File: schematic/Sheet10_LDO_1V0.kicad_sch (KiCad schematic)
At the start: 8 parts, among them U8 TPS7H1111-SP

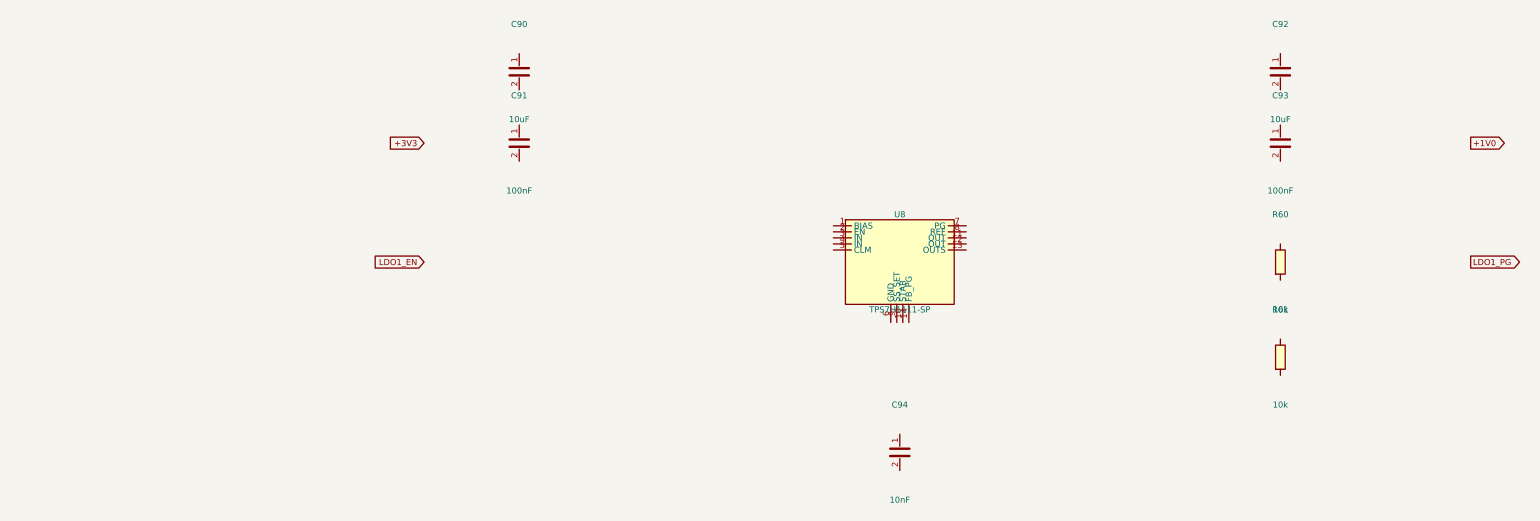
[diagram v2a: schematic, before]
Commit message: feat: add 745 wire connections linking all IC pins to labels and power symbols
- Added stub wires from every component pin to net labels/global_labels
- Power pins connected to correct power symbols (GND, +1V0, +1V8, +3V3, etc.)
- Signal pins connected to labeled nets matching design spec
- Global labels for cross-sheet signals (JESD, SPI, clock, SpaceWire)
- Fixed missing +3V3 power symbol definitions in 5 sheets
- All 17 sheets export successfully with KiCad CLI (17/17 OK)
- Merged PDF: 3.1MB, 17 pages with visible wire connections
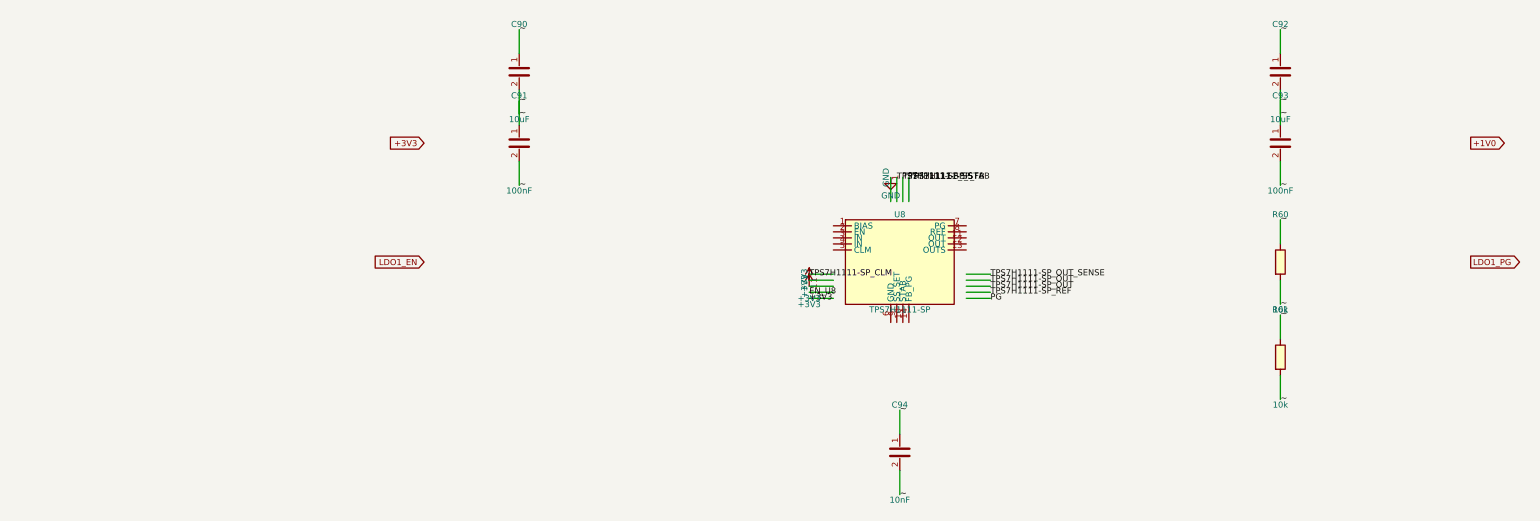
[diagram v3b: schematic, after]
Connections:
- net ~: now reaches C91.1
- net ~: now also C90.1, C90.2, C91.2, C92.1, C92.2, C93.1, C93.2, C94.1, C94.2, R60.1, R60.2, R61.1, R61.2
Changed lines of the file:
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@@
     (pin "1")
     (pin "2")
-  )  (global_label "+3V3" (shape input) (at 100 55 180) (effects (font (size 1.27 1.27)) (justify right)))  (global_label "+1V0" (shape output) (at 320 55 0) (effects (font (size 1.27 1.27)) (justify left)))  (global_label "LDO1_EN" (shape input) (at 100 80 180) (effects (font (size 1.27 1.27)) (justify right)))  (global_label "LDO1_PG" (shape output) (at 320 80 0) (effects (font (size 1.27 1.27)) (justify left)))  (sheet_instances (path "/" (page "1")))
+  )  (global_label "+3V3" (shape input) (at 100 55 180) (effects (font (size 1.27 1.27)) (justify right)))  (global_label "+1V0" (shape output) (at 320 55 0) (effects (font (size 1.27 1.27)) (justify left)))  (global_label "LDO1_EN" (shape input) (at 100 80 180) (effects (font (size 1.27 1.27)) (justify right)))  (global_label "LDO1_PG" (shape output) (at 320 80 0) (effects (font (size 1.27 1.27)) (justify left)))
+  (wire (pts (xy 186.03 87.62) (xy 180.95 87.62)) (stroke (width 0) (type default)))
+  (label "+3V3" (at 180.95 87.62 0) (effects (font (size 1.27 1.27))))
+  (wire (pts (xy 186.03 86.35) (xy 180.95 86.35)) (stroke (width 0) (type default)))
+  (label "EN_U8" (at 180.95 86.35 0) (effects (font (size 1.27 1.27))))
+  (wire (pts (xy 186.03 85.08) (xy 180.95 85.08)) (stroke (width 0) (type default)))
+  (symbol (lib_id "power:+3V3") (at 180.95 85.08 0) (unit 1)
+      (in_bom yes) (on_board yes) (dnp no)
+      (property "Reference" "#PWR6b4" (at 180.95 81.27 0) (effects (font (size 1.27 1.27)) hide))
+      (property "Value" "+3V3" (at 180.95 88.89 0) (effects (font (size 1.27 1.27))))
+      (property "Footprint" "" (at 0 0 0) (effects (font (size 1.27 1.27)) hide))
+      (property "Datasheet" "" (at 0 0 0) (effects (font (size 1.27 1.27)) hide))
+      (pin "1")
+    )
+  (wire (pts (xy 186.03 83.81) (xy 180.95 83.81)) (stroke (width 0) (type default)))
+  (symbol (lib_id "power:+3V3") (at 180.95 83.81 0) (unit 1)
+      (in_bom yes) (on_board yes) (dnp no)
+      (property "Reference" "#PWR41b" (at 180.95 80.00 0) (effects (font (size 1.27 1.27)) hide))
+      (property "Value" "+3V3" (at 180.95 87.62 0) (effects (font (size 1.27 1.27))))
+      (property "Footprint" "" (at 0 0 0) (effects (font (size 1.27 1.27)) hide))
+      (property "Datasheet" "" (at 0 0 0) (effects (font (size 1.27 1.27)) hide))
+      (pin "1")
+    )
+  (wire (pts (xy 186.03 82.54) (xy 180.95 82.54)) (stroke (width 0) (type default)))
+  (label "TPS7H1111-SP_CLM" (at 180.95 82.54 0) (effects (font (size 1.27 1.27))))
+  (wire (pts (xy 198.09 67.30) (xy 198.09 62.22)) (stroke (width 0) (type default)))
+  (symbol (lib_id "power:GND") (at 198.09 62.22 0) (unit 1)
+      (in_bom yes) (on_board yes) (dnp no)
+      (property "Reference" "#PWRbf7" (at 198.09 58.41 0) (effects (font (size 1.27 1.27)) hide))
+      (property "Value" "GND" (at 198.09 66.03 0) (effects (font (size 1.27 1.27))))
+      (property "Footprint" "" (at 0 0 0) (effects (font (size 1.27 1.27)) hide))
+      (property "Datasheet" "" (at 0 0 0) (effects (font (size 1.27 1.27)) hide))
+      (pin "1")
+    )
+  (wire (pts (xy 213.97 87.62) (xy 219.05 87.62)) (stroke (width 0) (type default)))
+  (label "PG" (at 219.05 87.62 0) (effects (font (size 1.27 1.27))))
+  (wire (pts (xy 213.97 86.35) (xy 219.05 86.35)) (stroke (width 0) (type default)))
+  (label "TPS7H1111-SP_REF" (at 219.05 86.35 0) (effects (font (size 1.27 1.27))))
+  (wire (pts (xy 199.37 67.30) (xy 199.37 62.22)) (stroke (width 0) (type default)))
+  (label "TPS7H1111-SP_SS" (at 199.37 62.22 0) (effects (font (size 1.27 1.27))))
+  (wire (pts (xy 200.63 67.30) (xy 200.63 62.22)) (stroke (width 0) (type default)))
+  (label "TPS7H1111-SP_STAB" (at 200.63 62.22 0) (effects (font (size 1.27 1.27))))
+  (wire (pts (xy 213.97 85.08) (xy 219.05 85.08)) (stroke (width 0) (type default)))
+  (label "TPS7H1111-SP_OUT" (at 219.05 85.08 0) (effects (font (size 1.27 1.27))))
+  (wire (pts (xy 213.97 83.81) (xy 219.05 83.81)) (stroke (width 0) (type default)))
+  (label "TPS7H1111-SP_OUT" (at 219.05 83.81 0) (effects (font (size 1.27 1.27))))
+  (wire (pts (xy 213.97 82.54) (xy 219.05 82.54)) (stroke (width 0) (type default)))
+  (label "TPS7H1111-SP_OUT_SENSE" (at 219.05 82.54 0) (effects (font (size 1.27 1.27))))
+  (wire (pts (xy 201.91 67.30) (xy 201.91 62.22)) (stroke (width 0) (type default)))
+  (label "TPS7H1111-SP_FB" (at 201.91 62.22 0) (effects (font (size 1.27 1.27))))
+  (wire (pts (xy 120.00 43.81) (xy 120.00 48.89)) (stroke (width 0) (type default)))
+  (label "~" (at 120.00 48.89 0) (effects (font (size 1.27 1.27))))
+  (wire (pts (xy 120.00 36.19) (xy 120.00 31.11)) (stroke (width 0) (type default)))
+  (label "~" (at 120.00 31.11 0) (effects (font (size 1.27 1.27))))
+  (wire (pts (xy 120.00 58.81) (xy 120.00 63.89)) (stroke (width 0) (type default)))
+  (label "~" (at 120.00 63.89 0) (effects (font (size 1.27 1.27))))
+  (wire (pts (xy 120.00 51.19) (xy 120.00 46.11)) (stroke (width 0) (type default)))
+  (label "~" (at 120.00 46.11 0) (effects (font (size 1.27 1.27))))
+  (wire (pts (xy 280.00 43.81) (xy 280.00 48.89)) (stroke (width 0) (type default)))
+  (label "~" (at 280.00 48.89 0) (effects (font (size 1.27 1.27))))
+  (wire (pts (xy 280.00 36.19) (xy 280.00 31.11)) (stroke (width 0) (type default)))
+  (label "~" (at 280.00 31.11 0) (effects (font (size 1.27 1.27))))
+  (wire (pts (xy 280.00 58.81) (xy 280.00 63.89)) (stroke (width 0) (type default)))
+  (label "~" (at 280.00 63.89 0) (effects (font (size 1.27 1.27))))
+  (wire (pts (xy 280.00 51.19) (xy 280.00 46.11)) (stroke (width 0) (type default)))
+  (label "~" (at 280.00 46.11 0) (effects (font (size 1.27 1.27))))
+  (wire (pts (xy 200.00 123.81) (xy 200.00 128.89)) (stroke (width 0) (type default)))
+  (label "~" (at 200.00 128.89 0) (effects (font (size 1.27 1.27))))
+  (wire (pts (xy 200.00 116.19) (xy 200.00 111.11)) (stroke (width 0) (type default)))
+  (label "~" (at 200.00 111.11 0) (effects (font (size 1.27 1.27))))
+  (wire (pts (xy 280.00 83.81) (xy 280.00 88.89)) (stroke (width 0) (type default)))
+  (label "~" (at 280.00 88.89 0) (effects (font (size 1.27 1.27))))
+  (wire (pts (xy 280.00 76.19) (xy 280.00 71.11)) (stroke (width 0) (type default)))
+  (label "~" (at 280.00 71.11 0) (effects (font (size 1.27 1.27))))
+  (wire (pts (xy 280.00 103.81) (xy 280.00 108.89)) (stroke (width 0) (type default)))
+  (label "~" (at 280.00 108.89 0) (effects (font (size 1.27 1.27))))
+  (wire (pts (xy 280.00 96.19) (xy 280.00 91.11)) (stroke (width 0) (type default)))
+  (label "~" (at 280.00 91.11 0) (effects (font (size 1.27 1.27))))
+  (sheet_instances (path "/" (page "1")))
 )

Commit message: Fix KiCad schematic wiring: Y-inversion bug + all 891 pins connected
- Fixed critical Y-axis inversion bug: KiCad inverts Y when placing
  symbols (lib Y + schematic Y = abs Y is WRONG; correct: abs Y = sym Y - lib Y)
- This caused ALL wires to connect to wrong pins (e.g., CS label connected
  to BG pin instead of CS pin)
- Verified with netlist: 0 unconnected nets, all pin functions correct
- Fixed wire direction for angle 90/270 (swapped due to Y-inversion)
- 891 pin connections across 15 sheets, all 17 sheets export without errors
- Netlist verification: CS→E8, BG→C3, INA+→A4, CLK+→F1, JESD pairs correct

Co-Authored-By: opencode <noreply@opencode.ai>
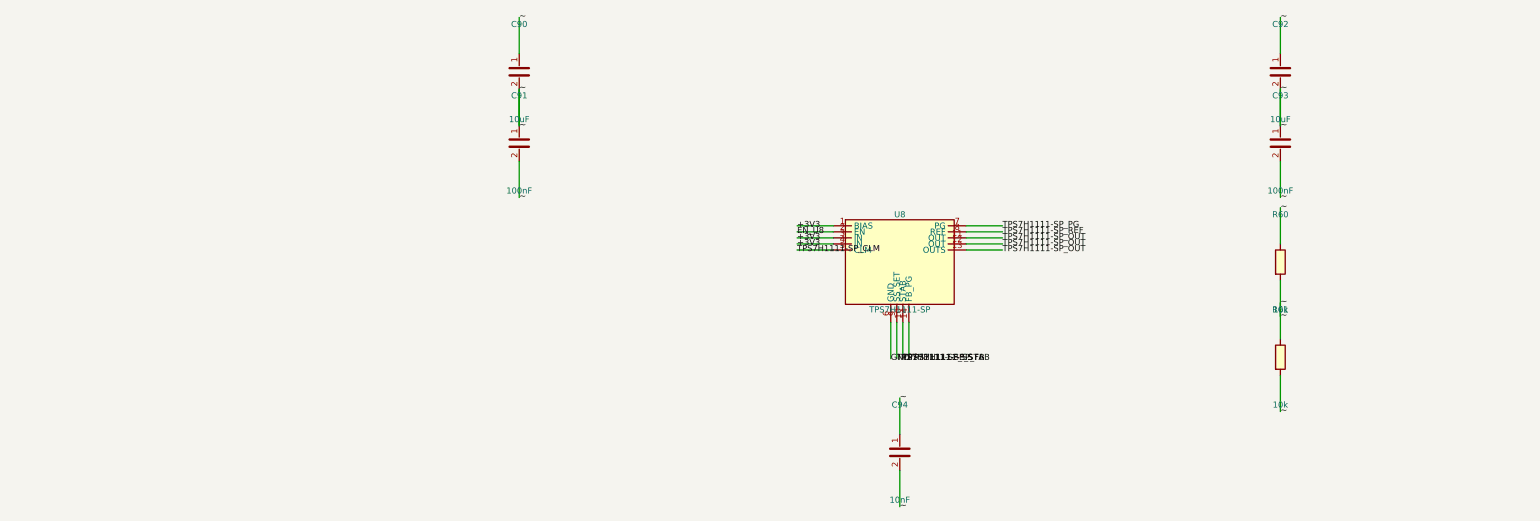
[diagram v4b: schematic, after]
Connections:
- net +3V3: now also U8.1 (BIAS), U8.3 (IN), U8.4 (IN)
- net EN_U8: now also U8.2 (EN)
- net GND: now also U8.6 (GND)
- net TPS7H1111-SP_CLM: now also U8.5 (CLM)
- net TPS7H1111-SP_FB: now also U8.14 (FB_PG)
- net TPS7H1111-SP_OUT: now also U8.11 (OUT), U8.12 (OUT), U8.13 (OUTS)
- net TPS7H1111-SP_REF: now also U8.8 (REF)
- net TPS7H1111-SP_SS: now also U8.9 (SS_SET)
- net TPS7H1111-SP_STAB: now also U8.10 (STAB)
- net TPS7H1111-SP_PG: now reaches U8.7 (PG)

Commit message: fix: replace wire stubs with labels-only to prevent power net shorts
Labels placed directly at pin endpoints eliminate wire overlap that
caused BGA power pins (VA11, VA19, VD11, AGND, DGND) to merge into
a single net. Verified via netlist: GND=52, +1V0_ANA=12, +1V9_ANA=12,
+1V1_DIG=10 nodes (all correct per datasheet pin mapping).
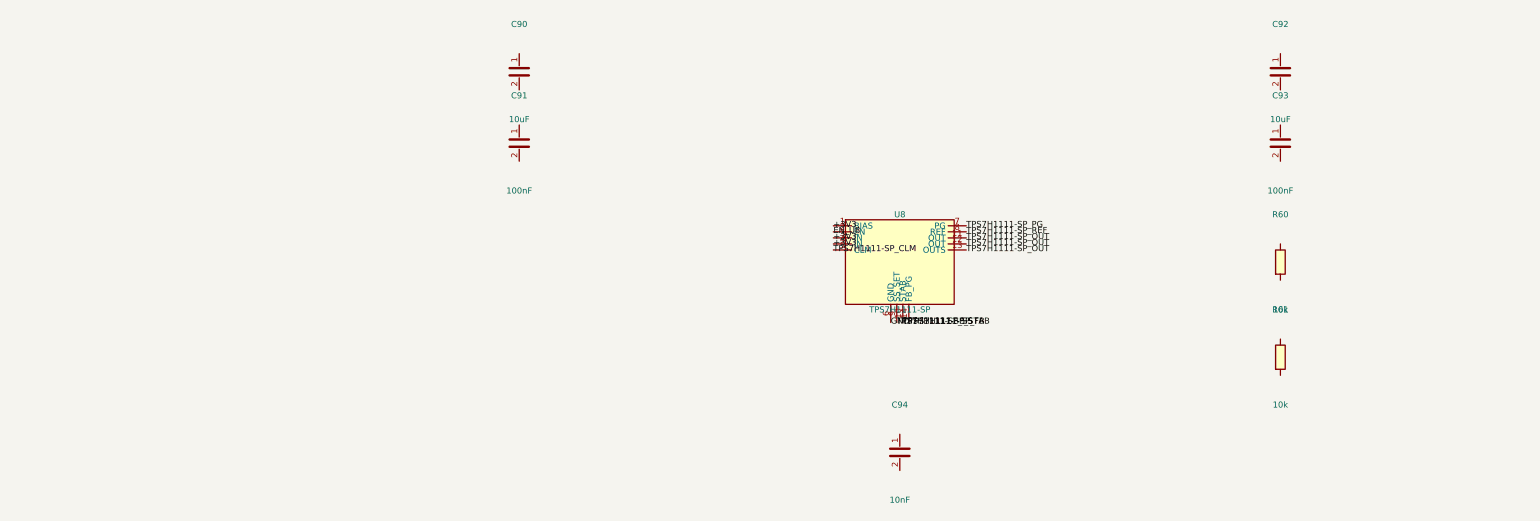
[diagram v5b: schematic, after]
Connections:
- removed net ~: C90.1, C90.2, C91.1, C91.2, C92.1, C92.2, C93.1, C93.2, C94.1, C94.2, R60.1, R60.2, R61.1, R61.2
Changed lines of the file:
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@@
     (pin "2")
   )
-  (wire (pts (xy 186.0300 72.3800) (xy 178.4100 72.3800)) (stroke (width 0) (type default)))
-  (label "+3V3" (at 178.4100 72.3800 0) (effects (font (size 1.27 1.27))))
-  (wire (pts (xy 186.0300 73.6500) (xy 178.4100 73.6500)) (stroke (width 0) (type default)))
-  (label "EN_U8" (at 178.4100 73.6500 0) (effects (font (size 1.27 1.27))))
-  (wire (pts (xy 186.0300 74.9200) (xy 178.4100 74.9200)) (stroke (width 0) (type default)))
-  (label "+3V3" (at 178.4100 74.9200 0) (effects (font (size 1.27 1.27))))
-  (wire (pts (xy 186.0300 76.1900) (xy 178.4100 76.1900)) (stroke (width 0) (type default)))
-  (label "+3V3" (at 178.4100 76.1900 0) (effects (font (size 1.27 1.27))))
-  (wire (pts (xy 186.0300 77.4600) (xy 178.4100 77.4600)) (stroke (width 0) (type default)))
-  (label "TPS7H1111-SP_CLM" (at 178.4100 77.4600 0) (effects (font (size 1.27 1.27))))
-  (wire (pts (xy 213.9700 72.3800) (xy 221.5900 72.3800)) (stroke (width 0) (type default)))
-  (label "TPS7H1111-SP_PG" (at 221.5900 72.3800 0) (effects (font (size 1.27 1.27))))
-  (wire (pts (xy 213.9700 73.6500) (xy 221.5900 73.6500)) (stroke (width 0) (type default)))
-  (label "TPS7H1111-SP_REF" (at 221.5900 73.6500 0) (effects (font (size 1.27 1.27))))
-  (wire (pts (xy 213.9700 74.9200) (xy 221.5900 74.9200)) (stroke (width 0) (type default)))
-  (label "TPS7H1111-SP_OUT" (at 221.5900 74.9200 0) (effects (font (size 1.27 1.27))))
-  (wire (pts (xy 213.9700 76.1900) (xy 221.5900 76.1900)) (stroke (width 0) (type default)))
-  (label "TPS7H1111-SP_OUT" (at 221.5900 76.1900 0) (effects (font (size 1.27 1.27))))
-  (wire (pts (xy 213.9700 77.4600) (xy 221.5900 77.4600)) (stroke (width 0) (type default)))
-  (label "TPS7H1111-SP_OUT" (at 221.5900 77.4600 0) (effects (font (size 1.27 1.27))))
-  (wire (pts (xy 198.0950 92.7000) (xy 198.0950 100.3200)) (stroke (width 0) (type default)))
-  (label "GND" (at 198.0950 100.3200 0) (effects (font (size 1.27 1.27))))
-  (wire (pts (xy 199.3650 92.7000) (xy 199.3650 100.3200)) (stroke (width 0) (type default)))
-  (label "TPS7H1111-SP_SS" (at 199.3650 100.3200 0) (effects (font (size 1.27 1.27))))
-  (wire (pts (xy 200.6350 92.7000) (xy 200.6350 100.3200)) (stroke (width 0) (type default)))
-  (label "TPS7H1111-SP_STAB" (at 200.6350 100.3200 0) (effects (font (size 1.27 1.27))))
-  (wire (pts (xy 201.9050 92.7000) (xy 201.9050 100.3200)) (stroke (width 0) (type default)))
-  (label "TPS7H1111-SP_FB" (at 201.9050 100.3200 0) (effects (font (size 1.27 1.27))))
-  (wire (pts (xy 120.0000 36.1900) (xy 120.0000 28.5700)) (stroke (width 0) (type default)))
-  (label "~" (at 120.0000 28.5700 0) (effects (font (size 1.27 1.27))))
-  (wire (pts (xy 120.0000 43.8100) (xy 120.0000 51.4300)) (stroke (width 0) (type default)))
-  (label "~" (at 120.0000 51.4300 0) (effects (font (size 1.27 1.27))))
-  (wire (pts (xy 120.0000 51.1900) (xy 120.0000 43.5700)) (stroke (width 0) (type default)))
-  (label "~" (at 120.0000 43.5700 0) (effects (font (size 1.27 1.27))))
-  (wire (pts (xy 120.0000 58.8100) (xy 120.0000 66.4300)) (stroke (width 0) (type default)))
-  (label "~" (at 120.0000 66.4300 0) (effects (font (size 1.27 1.27))))
-  (wire (pts (xy 280.0000 36.1900) (xy 280.0000 28.5700)) (stroke (width 0) (type default)))
-  (label "~" (at 280.0000 28.5700 0) (effects (font (size 1.27 1.27))))
-  (wire (pts (xy 280.0000 43.8100) (xy 280.0000 51.4300)) (stroke (width 0) (type default)))
-  (label "~" (at 280.0000 51.4300 0) (effects (font (size 1.27 1.27))))
-  (wire (pts (xy 280.0000 51.1900) (xy 280.0000 43.5700)) (stroke (width 0) (type default)))
-  (label "~" (at 280.0000 43.5700 0) (effects (font (size 1.27 1.27))))
-  (wire (pts (xy 280.0000 58.8100) (xy 280.0000 66.4300)) (stroke (width 0) (type default)))
-  (label "~" (at 280.0000 66.4300 0) (effects (font (size 1.27 1.27))))
-  (wire (pts (xy 200.0000 116.1900) (xy 200.0000 108.5700)) (stroke (width 0) (type default)))
-  (label "~" (at 200.0000 108.5700 0) (effects (font (size 1.27 1.27))))
-  (wire (pts (xy 200.0000 123.8100) (xy 200.0000 131.4300)) (stroke (width 0) (type default)))
-  (label "~" (at 200.0000 131.4300 0) (effects (font (size 1.27 1.27))))
-  (wire (pts (xy 280.0000 76.1900) (xy 280.0000 68.5700)) (stroke (width 0) (type default)))
-  (label "~" (at 280.0000 68.5700 0) (effects (font (size 1.27 1.27))))
-  (wire (pts (xy 280.0000 83.8100) (xy 280.0000 91.4300)) (stroke (width 0) (type default)))
-  (label "~" (at 280.0000 91.4300 0) (effects (font (size 1.27 1.27))))
-  (wire (pts (xy 280.0000 96.1900) (xy 280.0000 88.5700)) (stroke (width 0) (type default)))
-  (label "~" (at 280.0000 88.5700 0) (effects (font (size 1.27 1.27))))
-  (wire (pts (xy 280.0000 103.8100) (xy 280.0000 111.4300)) (stroke (width 0) (type default)))
-  (label "~" (at 280.0000 111.4300 0) (effects (font (size 1.27 1.27))))
+  (label "+3V3" (at 186.0300 72.3800 0) (effects (font (size 1.27 1.27))))
+  (label "EN_U8" (at 186.0300 73.6500 0) (effects (font (size 1.27 1.27))))
+  (label "+3V3" (at 186.0300 74.9200 0) (effects (font (size 1.27 1.27))))
+  (label "+3V3" (at 186.0300 76.1900 0) (effects (font (size 1.27 1.27))))
+  (label "TPS7H1111-SP_CLM" (at 186.0300 77.4600 0) (effects (font (size 1.27 1.27))))
+  (label "TPS7H1111-SP_PG" (at 213.9700 72.3800 0) (effects (font (size 1.27 1.27))))
+  (label "TPS7H1111-SP_REF" (at 213.9700 73.6500 0) (effects (font (size 1.27 1.27))))
+  (label "TPS7H1111-SP_OUT" (at 213.9700 74.9200 0) (effects (font (size 1.27 1.27))))
+  (label "TPS7H1111-SP_OUT" (at 213.9700 76.1900 0) (effects (font (size 1.27 1.27))))
+  (label "TPS7H1111-SP_OUT" (at 213.9700 77.4600 0) (effects (font (size 1.27 1.27))))
+  (label "GND" (at 198.0950 92.7000 0) (effects (font (size 1.27 1.27))))
+  (label "TPS7H1111-SP_SS" (at 199.3650 92.7000 0) (effects (font (size 1.27 1.27))))
+  (label "TPS7H1111-SP_STAB" (at 200.6350 92.7000 0) (effects (font (size 1.27 1.27))))
+  (label "TPS7H1111-SP_FB" (at 201.9050 92.7000 0) (effects (font (size 1.27 1.27))))
   (sheet_instances (path "/" (page "1")))
 )
